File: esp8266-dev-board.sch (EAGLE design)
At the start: 9 parts

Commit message: Fix sch warnings
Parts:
- D1: value (none) -> red
- J1: value (none) -> left
- J2: value (none) -> right
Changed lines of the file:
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@@
 <?xml version="1.0" encoding="utf-8"?>
 <!DOCTYPE eagle SYSTEM "eagle.dtd">
-<eagle version="7.3.0">
+<eagle version="9.2.2">
 <drawing>
 <settings>
 <setting alwaysvectorfont="no"/>
+<setting keepoldvectorfont="yes"/>
 <setting verticaltext="up"/>
 </settings>
-<grid distance="0.1" unitdist="inch" unit="inch" style="lines" multiple="1" display="no" altdistance="0.01" altunitdist="inch" altunit="inch"/>
+<grid distance="0.01" unitdist="inch" unit="inch" style="lines" multiple="1" display="no" altdistance="0.01" altunitdist="inch" altunit="inch"/>
 <layers>
 <layer number="1" name="Top" color="4" fill="1" visible="no" active="no"/>
@@
 </classes>
 <parts>
-<part name="J1" library="SparkFun-Connectors" deviceset="M08" device=""/>
-<part name="J2" library="SparkFun-Connectors" deviceset="M08" device=""/>
+<part name="J1" library="SparkFun-Connectors" deviceset="M08" device="" value="left"/>
+<part name="J2" library="SparkFun-Connectors" deviceset="M08" device="" value="right"/>
 <part name="GND1" library="SparkFun-Aesthetics" deviceset="GND" device=""/>
 <part name="S1" library="SparkFun-Switches" deviceset="MOMENTARY-SWITCH-SPST" device="-SMD-6.0X3.5MM" value=""/>
@@
 <part name="GND3" library="SparkFun-Aesthetics" deviceset="GND" device=""/>
 <part name="U$1" library="arcadetv" deviceset="EXT-PORT-AGB" device=""/>
-<part name="D1" library="SparkFun-LED" deviceset="LED" device="0603"/>
+<part name="D1" library="SparkFun-LED" deviceset="LED" device="0603" value="red"/>
 <part name="R1" library="SparkFun-Resistors" deviceset="RESISTOR" device="0805" value=" "/>
 <part name="R2" library="SparkFun-Resistors" deviceset="RESISTOR" device="0805" value=" "/>
@@
 <part name="SUPPLY3" library="SparkFun-PowerSymbols" deviceset="VCC" device=""/>
 <part name="C1" library="SparkFun-Capacitors" deviceset="10UF" device="-0805-10V-10%" value="10uF"/>
-<part name="FRAME1" library="frames" deviceset="A4L-LOC" device=""/>
+<part name="FRAME1" library="frames" deviceset="A4L-LOC" device="" value="default"/>
 </parts>
 <sheets>
@@
 </plain>
 <instances>
-<instance part="J1" gate="G$1" x="101.6" y="96.52"/>
-<instance part="J2" gate="G$1" x="172.72" y="96.52" rot="MR0"/>
-<instance part="GND1" gate="1" x="119.38" y="76.2"/>
-<instance part="S1" gate="G$1" x="78.74" y="88.9" rot="R270"/>
+<instance part="J1" gate="G$1" x="101.6" y="96.52" smashed="yes">
+<attribute name="VALUE" x="96.52" y="83.82" size="1.778" layer="96"/>
+<attribute name="NAME" x="96.52" y="109.982" size="1.778" layer="95" display="off"/>
+</instance>
+<instance part="J2" gate="G$1" x="172.72" y="96.52" smashed="yes" rot="MR0">
+<attribute name="VALUE" x="177.8" y="83.82" size="1.778" layer="96" rot="MR0"/>
+<attribute name="NAME" x="177.8" y="109.982" size="1.778" layer="95" rot="MR0"/>
+</instance>
+<instance part="GND1" gate="1" x="119.38" y="76.2" smashed="yes">
+<attribute name="VALUE" x="116.84" y="73.66" size="1.778" layer="96"/>
+</instance>
+<instance part="S1" gate="G$1" x="78.74" y="88.9" smashed="yes" rot="R270">
+<attribute name="NAME" x="80.264" y="88.9" size="1.778" layer="95" font="vector" rot="R270" align="bottom-center"/>
+<attribute name="VALUE" x="78.232" y="88.9" size="1.778" layer="96" font="vector" rot="R270" align="top-center"/>
+</instance>
 <instance part="PRGM" gate="G$1" x="68.58" y="96.52" smashed="yes" rot="R270">
 <attribute name="NAME" x="70.104" y="96.52" size="1.778" layer="95" font="vector" rot="R270" align="bottom-center"/>
 <attribute name="VALUE" x="68.072" y="96.52" size="1.778" layer="96" font="vector" rot="R270" align="top-center"/>
 </instance>
-<instance part="GND2" gate="1" x="68.58" y="76.2"/>
-<instance part="GND3" gate="1" x="78.74" y="76.2"/>
-<instance part="U$1" gate="G$1" x="137.16" y="93.98" rot="MR0"/>
-<instance part="D1" gate="G$1" x="187.96" y="88.9"/>
-<instance part="R1" gate="G$1" x="187.96" y="99.06" rot="R90"/>
-<instance part="R2" gate="G$1" x="78.74" y="101.6" rot="R90"/>
-<instance part="SUPPLY1" gate="G$1" x="154.94" y="109.22"/>
-<instance part="SUPPLY2" gate="G$1" x="78.74" y="109.22"/>
-<instance part="SUPPLY3" gate="G$1" x="187.96" y="109.22"/>
-<instance part="C1" gate="G$1" x="86.36" y="86.36"/>
-<instance part="FRAME1" gate="G$1" x="0" y="0"/>
+<instance part="GND2" gate="1" x="68.58" y="76.2" smashed="yes">
+<attribute name="VALUE" x="66.04" y="73.66" size="1.778" layer="96"/>
+</instance>
+<instance part="GND3" gate="1" x="78.74" y="76.2" smashed="yes">
+<attribute name="VALUE" x="76.2" y="73.66" size="1.778" layer="96"/>
+</instance>
+<instance part="U$1" gate="G$1" x="137.16" y="93.98" smashed="yes" rot="MR0"/>
+<instance part="D1" gate="G$1" x="187.96" y="88.9" smashed="yes">
+<attribute name="NAME" x="184.531" y="84.328" size="1.778" layer="95" font="vector" rot="R90"/>
+<attribute name="VALUE" x="189.865" y="85.598" size="1.778" layer="96" font="vector" rot="R90" align="top-left"/>
+</instance>
+<instance part="R1" gate="G$1" x="187.96" y="99.06" smashed="yes" rot="R90">
+<attribute name="NAME" x="186.436" y="99.06" size="1.778" layer="95" font="vector" rot="R90" align="bottom-center"/>
+<attribute name="VALUE" x="189.484" y="99.06" size="1.778" layer="96" font="vector" rot="R90" align="top-center"/>
+</instance>
+<instance part="R2" gate="G$1" x="78.74" y="101.6" smashed="yes" rot="R90">
+<attribute name="NAME" x="77.216" y="101.6" size="1.778" layer="95" font="vector" rot="R90" align="bottom-center"/>
+<attribute name="VALUE" x="80.264" y="101.6" size="1.778" layer="96" font="vector" rot="R90" align="top-center"/>
+</instance>
+<instance part="SUPPLY1" gate="G$1" x="154.94" y="109.22" smashed="yes">
+<attribute name="VALUE" x="154.94" y="112.014" size="1.778" layer="96" align="bottom-center"/>
+</instance>
+<instance part="SUPPLY2" gate="G$1" x="78.74" y="109.22" smashed="yes">
+<attribute name="VALUE" x="78.74" y="112.014" size="1.778" layer="96" align="bottom-center"/>
+</instance>
+<instance part="SUPPLY3" gate="G$1" x="187.96" y="109.22" smashed="yes">
+<attribute name="VALUE" x="187.96" y="112.014" size="1.778" layer="96" align="bottom-center"/>
+</instance>
+<instance part="C1" gate="G$1" x="86.36" y="86.36" smashed="yes">
+<attribute name="NAME" x="87.884" y="89.281" size="1.778" layer="95" font="vector"/>
+<attribute name="VALUE" x="87.884" y="84.201" size="1.778" layer="96" font="vector"/>
+</instance>
+<instance part="FRAME1" gate="G$1" x="0" y="0" smashed="yes">
+<attribute name="DRAWING_NAME" x="217.17" y="15.24" size="2.54" layer="94"/>
+<attribute name="LAST_DATE_TIME" x="217.17" y="10.16" size="2.286" layer="94"/>
+<attribute name="SHEET" x="230.505" y="5.08" size="2.54" layer="94"/>
+</instance>
 </instances>
 <busses>
@@
 <pinref part="U$1" gate="G$1" pin="GND"/>
 <pinref part="U$1" gate="G$1" pin="SHIELD"/>
+<junction x="119.38" y="93.98"/>
+<junction x="119.38" y="91.44"/>
 </segment>
 <segment>
@@
 <wire x1="86.36" y1="81.28" x2="78.74" y2="81.28" width="0.1524" layer="91"/>
 <pinref part="C1" gate="G$1" pin="2"/>
+<junction x="78.74" y="81.28"/>
 </segment>
 </net>
@@
 <label x="83.566" y="95.25" size="1.778" layer="95"/>
 <pinref part="C1" gate="G$1" pin="1"/>
-</segment>
-</net>
+<junction x="78.74" y="95.25"/>
+</segment>
+</net>

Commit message: Fixed zero width polygons and top silkscreen
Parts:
- R1, R2: value (none) -> 4.7k
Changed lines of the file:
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@@
 <part name="U$1" library="arcadetv" deviceset="EXT-PORT-AGB" device=""/>
 <part name="D1" library="SparkFun-LED" deviceset="LED" device="0603" value="red"/>
-<part name="R1" library="SparkFun-Resistors" deviceset="RESISTOR" device="0805" value=" "/>
-<part name="R2" library="SparkFun-Resistors" deviceset="RESISTOR" device="0805" value=" "/>
+<part name="R1" library="SparkFun-Resistors" deviceset="RESISTOR" device="0805" value=" 4.7k"/>
+<part name="R2" library="SparkFun-Resistors" deviceset="RESISTOR" device="0805" value="4.7k"/>
 <part name="SUPPLY1" library="SparkFun-PowerSymbols" deviceset="VCC" device=""/>
 <part name="SUPPLY2" library="SparkFun-PowerSymbols" deviceset="VCC" device=""/>

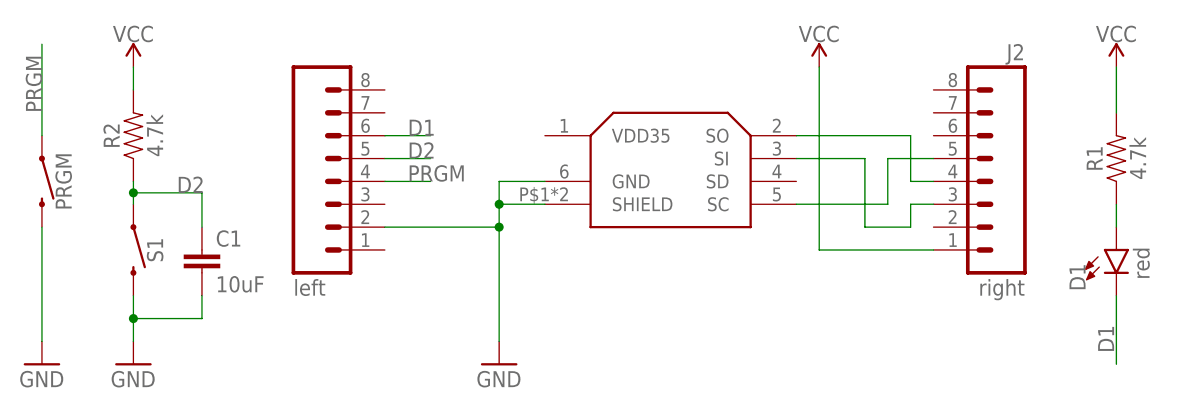
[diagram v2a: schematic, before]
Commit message: MicroSD shield compatibility
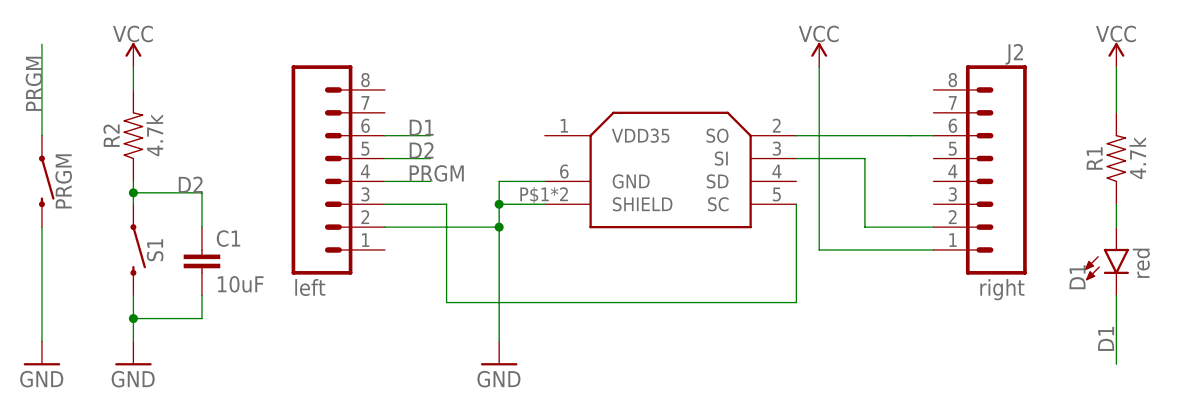
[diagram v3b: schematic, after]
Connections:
- net N$1: now also J1.3; no longer J2.5
- net N$2: now also J2.6; no longer J2.4
- net N$3: now also J2.2; no longer J2.3
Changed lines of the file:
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@@
-</segment>
-</net>
-<net name="N$1" class="0">
-<segment>
-<pinref part="J2" gate="G$1" pin="5"/>
-<wire x1="167.64" y1="99.06" x2="162.56" y2="99.06" width="0.1524" layer="91"/>
-<wire x1="162.56" y1="99.06" x2="162.56" y2="93.98" width="0.1524" layer="91"/>
-<wire x1="162.56" y1="93.98" x2="152.4" y2="93.98" width="0.1524" layer="91"/>
-<pinref part="U$1" gate="G$1" pin="SC"/>
 </segment>
 </net>
@@
 <segment>
 <pinref part="U$1" gate="G$1" pin="SO"/>
-<wire x1="152.4" y1="101.6" x2="165.1" y2="101.6" width="0.1524" layer="91"/>
-<wire x1="165.1" y1="101.6" x2="165.1" y2="96.52" width="0.1524" layer="91"/>
-<pinref part="J2" gate="G$1" pin="4"/>
-<wire x1="165.1" y1="96.52" x2="167.64" y2="96.52" width="0.1524" layer="91"/>
+<wire x1="152.4" y1="101.6" x2="164.846" y2="101.6" width="0.1524" layer="91"/>
+<pinref part="J2" gate="G$1" pin="6"/>
+<wire x1="164.846" y1="101.6" x2="165.1" y2="101.6" width="0.1524" layer="91"/>
+<wire x1="165.1" y1="101.6" x2="167.64" y2="101.6" width="0.1524" layer="91"/>
 </segment>
 </net>
 <net name="N$3" class="0">
 <segment>
-<pinref part="J2" gate="G$1" pin="3"/>
-<wire x1="167.64" y1="93.98" x2="165.1" y2="93.98" width="0.1524" layer="91"/>
-<wire x1="165.1" y1="93.98" x2="165.1" y2="91.44" width="0.1524" layer="91"/>
-<wire x1="165.1" y1="91.44" x2="160.02" y2="91.44" width="0.1524" layer="91"/>
+<wire x1="167.64" y1="91.44" x2="160.02" y2="91.44" width="0.1524" layer="91"/>
 <wire x1="160.02" y1="91.44" x2="160.02" y2="99.06" width="0.1524" layer="91"/>
 <pinref part="U$1" gate="G$1" pin="SI"/>
 <wire x1="160.02" y1="99.06" x2="152.4" y2="99.06" width="0.1524" layer="91"/>
+<pinref part="J2" gate="G$1" pin="2"/>
 </segment>
 </net>
@@
 </segment>
 </net>
+<net name="N$1" class="0">
+<segment>
+<pinref part="J1" gate="G$1" pin="3"/>
+<wire x1="106.68" y1="93.98" x2="113.538" y2="93.98" width="0.1524" layer="91"/>
+<wire x1="113.538" y1="93.98" x2="113.538" y2="83.058" width="0.1524" layer="91"/>
+<pinref part="U$1" gate="G$1" pin="SC"/>
+<wire x1="113.538" y1="83.058" x2="152.4" y2="83.058" width="0.1524" layer="91"/>
+<wire x1="152.4" y1="83.058" x2="152.4" y2="93.98" width="0.1524" layer="91"/>
+</segment>
+</net>
